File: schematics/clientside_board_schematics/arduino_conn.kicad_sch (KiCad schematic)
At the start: 1 part

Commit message: Assign footprints to RLCS Client-side board
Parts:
- XA1: footprint (none) -> rlcs_power_footprints:Arduino_Mega2560_Shield
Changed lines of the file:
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@@
       (effects (font (size 1.524 1.524)))
     )
-    (property "Footprint" "" (id 2) (at 163.83 18.415 0)
+    (property "Footprint" "rlcs_power_footprints:Arduino_Mega2560_Shield" (id 2) (at 163.83 18.415 0)
       (effects (font (size 1.524 1.524)) hide)
     )

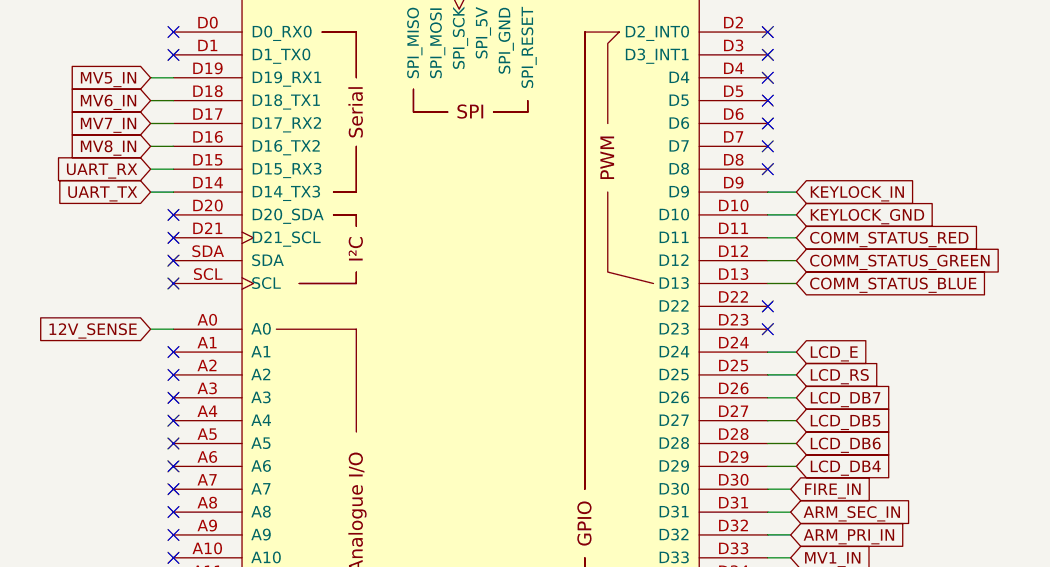
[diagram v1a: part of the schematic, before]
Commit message: Fix schematic issue on Client-side board
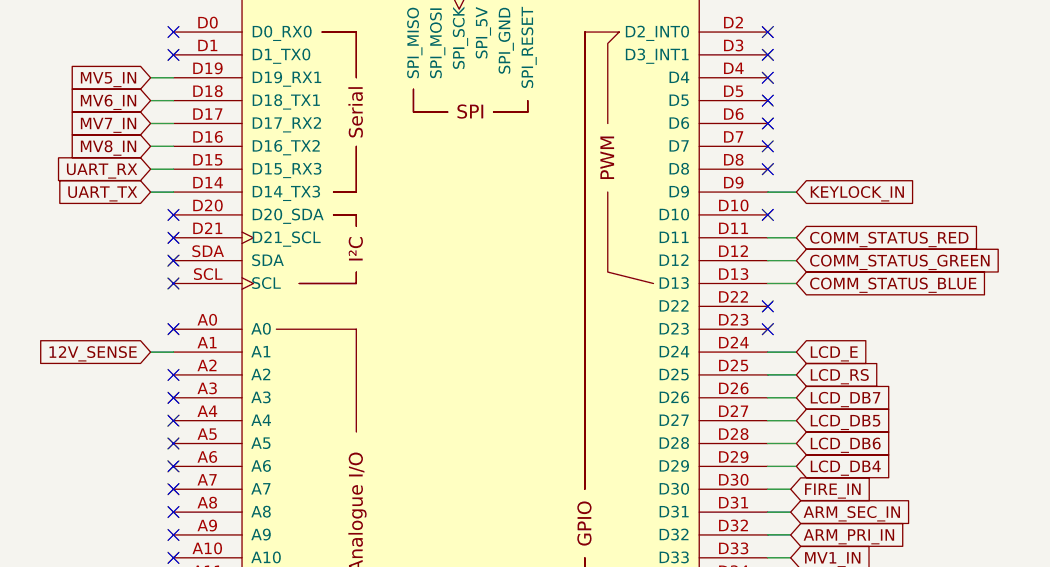
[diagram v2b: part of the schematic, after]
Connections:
- net 12V_SENSE: now also XA1.A1; no longer XA1.A0
- net KEYLOCK_GND: no longer names the net of XA1.D10
- no-connect marks 56 -> 57
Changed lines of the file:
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@@
   (no_connect (at 113.03 107.315))
   (no_connect (at 113.03 89.535))
-  (no_connect (at 113.03 69.215))
   (no_connect (at 113.03 53.975))
   (no_connect (at 179.07 36.195))
@@
   (no_connect (at 142.24 22.225))
   (no_connect (at 113.03 86.995))
+  (no_connect (at 113.03 66.675))
   (no_connect (at 179.07 117.475))
   (no_connect (at 179.07 140.335))
@@
   (no_connect (at 179.07 41.275))
   (no_connect (at 179.07 122.555))
+  (no_connect (at 179.07 53.975))
   (no_connect (at 113.03 104.775))
   (no_connect (at 179.07 43.815))
@@
     (stroke (width 0) (type default) (color 0 0 0 0))
   )
-  (wire (pts (xy 179.07 53.975) (xy 182.245 53.975))
-    (stroke (width 0) (type default) (color 0 0 0 0))
-  )
   (wire (pts (xy 108.585 135.255) (xy 108.585 137.795))
     (stroke (width 0) (type default) (color 0 0 0 0))
@@
     (stroke (width 0) (type default) (color 0 0 0 0))
   )
+  (wire (pts (xy 110.49 69.215) (xy 113.03 69.215))
+    (stroke (width 0) (type default) (color 0 0 0 0))
+  )
   (wire (pts (xy 179.07 59.055) (xy 182.245 59.055))
     (stroke (width 0) (type default) (color 0 0 0 0))
@@
     (stroke (width 0) (type default) (color 0 0 0 0))
   )
-  (wire (pts (xy 110.49 66.675) (xy 113.03 66.675))
-    (stroke (width 0) (type default) (color 0 0 0 0))
-  )
   (wire (pts (xy 108.585 137.795) (xy 108.585 140.335))
     (stroke (width 0) (type default) (color 0 0 0 0))
@@
     )
   )
-  (global_label "KEYLOCK_GND" (shape input) (at 182.245 53.975 0) (fields_autoplaced)
-    (effects (font (size 1.27 1.27)) (justify left))
-    (property "Intersheet References" "${INTERSHEET_REFS}" (id 0) (at 197.9024 53.8956 0)
-      (effects (font (size 1.27 1.27)) (justify left) hide)
-    )
-  )
   (global_label "ARM_SEC_IN" (shape input) (at 181.61 86.995 0) (fields_autoplaced)
     (effects (font (size 1.27 1.27)) (justify left))
@@
     )
   )
-  (global_label "12V_SENSE" (shape input) (at 110.49 66.675 180) (fields_autoplaced)
-    (effects (font (size 1.27 1.27)) (justify right))
-    (property "Intersheet References" "${INTERSHEET_REFS}" (id 0) (at 97.554 66.5956 0)
-      (effects (font (size 1.27 1.27)) (justify right) hide)
-    )
+  (global_label "12V_SENSE" (shape input) (at 110.49 69.215 180) (fields_autoplaced)
+    (effects (font (size 1.27 1.27)) (justify right))
+    (property "Intersheet References" "${INTERSHEET_REFS}" (id 0) (at 97.554 69.1356 0)
+      (effects (font (size 1.27 1.27)) (justify right) hide)
+    )

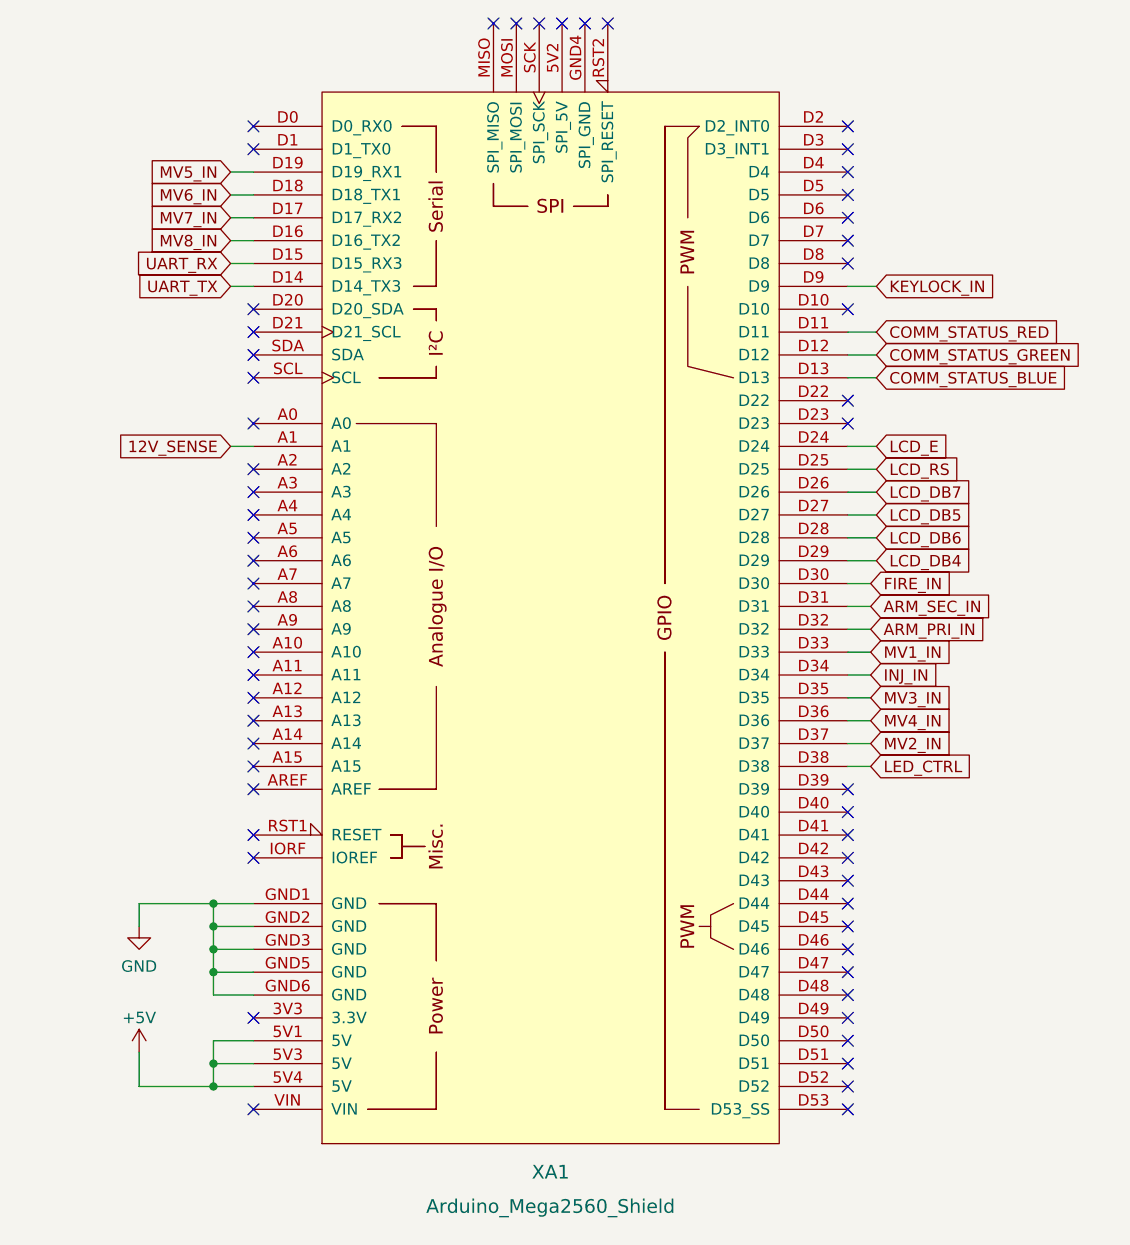
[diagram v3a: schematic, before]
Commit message: Update client-side board schematic
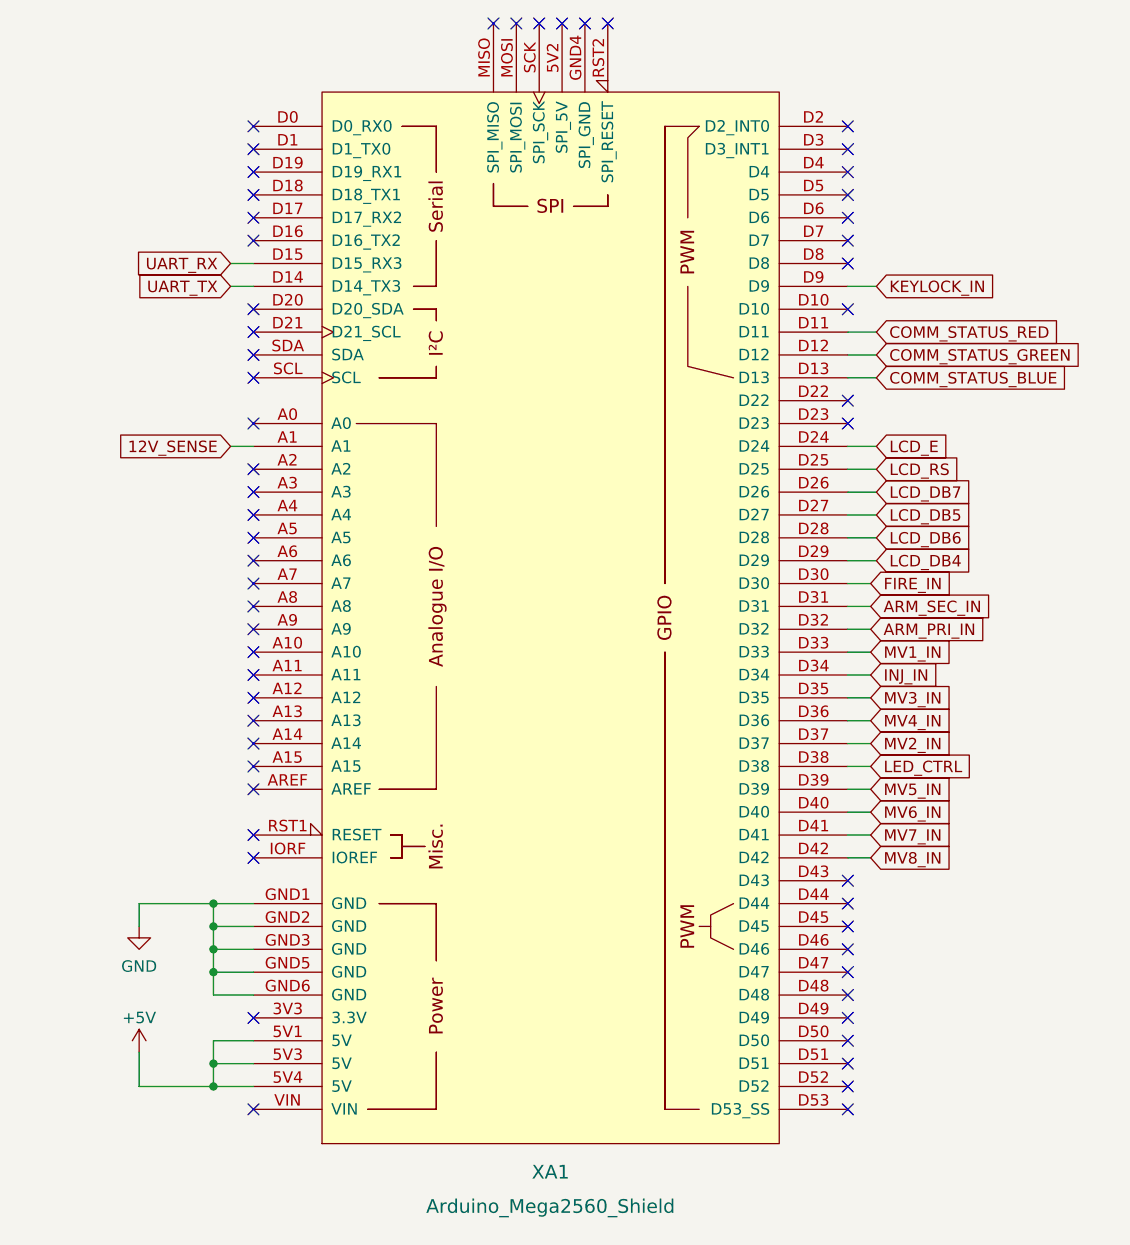
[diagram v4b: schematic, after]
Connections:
- net MV5_IN: now also XA1.D39; no longer XA1.D19 (D19_RX1)
- net MV6_IN: now also XA1.D40; no longer XA1.D18 (D18_TX1)
- net MV7_IN: now also XA1.D41; no longer XA1.D17 (D17_RX2)
- net MV8_IN: now also XA1.D42; no longer XA1.D16 (D16_TX2)
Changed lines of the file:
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@@
   (no_connect (at 113.03 59.055))
   (no_connect (at 179.07 127.635))
-  (no_connect (at 179.07 114.935))
   (no_connect (at 113.03 107.315))
   (no_connect (at 113.03 89.535))
@@
   (no_connect (at 179.07 48.895))
   (no_connect (at 147.32 22.225))
-  (no_connect (at 179.07 107.315))
   (no_connect (at 113.03 81.915))
   (no_connect (at 179.07 46.355))
   (no_connect (at 113.03 99.695))
-  (no_connect (at 179.07 112.395))
-  (no_connect (at 179.07 109.855))
   (no_connect (at 113.03 36.195))
   (no_connect (at 113.03 114.935))
@@
   (no_connect (at 179.07 142.875))
   (no_connect (at 179.07 41.275))
+  (no_connect (at 113.03 38.735))
   (no_connect (at 179.07 122.555))
+  (no_connect (at 113.03 43.815))
   (no_connect (at 179.07 53.975))
+  (no_connect (at 113.03 46.355))
   (no_connect (at 113.03 104.775))
   (no_connect (at 179.07 43.815))
   (no_connect (at 113.03 97.155))
   (no_connect (at 113.03 56.515))
+  (no_connect (at 113.03 41.275))
   (no_connect (at 113.03 71.755))
   (no_connect (at 179.07 33.655))
@@
   (no_connect (at 113.03 74.295))
   (no_connect (at 152.4 22.225))
-  (wire (pts (xy 110.49 38.735) (xy 113.03 38.735))
-    (stroke (width 0) (type default) (color 0 0 0 0))
-  )
   (wire (pts (xy 179.07 79.375) (xy 182.245 79.375))
     (stroke (width 0) (type default) (color 0 0 0 0))
@@
     (stroke (width 0) (type default) (color 0 0 0 0))
   )
+  (wire (pts (xy 179.07 112.395) (xy 181.61 112.395))
+    (stroke (width 0) (type default) (color 0 0 0 0))
+  )
   (wire (pts (xy 179.07 84.455) (xy 181.61 84.455))
     (stroke (width 0) (type default) (color 0 0 0 0))
@@
     (stroke (width 0) (type default) (color 0 0 0 0))
   )
-  (wire (pts (xy 110.49 43.815) (xy 113.03 43.815))
+  (wire (pts (xy 179.07 107.315) (xy 181.61 107.315))
     (stroke (width 0) (type default) (color 0 0 0 0))
   )
@@
     (stroke (width 0) (type default) (color 0 0 0 0))
   )
-  (wire (pts (xy 110.49 41.275) (xy 113.03 41.275))
-    (stroke (width 0) (type default) (color 0 0 0 0))
-  )
   (wire (pts (xy 108.585 127.635) (xy 113.03 127.635))
     (stroke (width 0) (type default) (color 0 0 0 0))
@@
     (stroke (width 0) (type default) (color 0 0 0 0))
   )
+  (wire (pts (xy 179.07 114.935) (xy 181.61 114.935))
+    (stroke (width 0) (type default) (color 0 0 0 0))
+  )
   (wire (pts (xy 179.07 97.155) (xy 181.61 97.155))
     (stroke (width 0) (type default) (color 0 0 0 0))
@@
     (stroke (width 0) (type default) (color 0 0 0 0))
   )
-  (wire (pts (xy 110.49 46.355) (xy 113.03 46.355))
-    (stroke (width 0) (type default) (color 0 0 0 0))
-  )
   (wire (pts (xy 108.585 140.335) (xy 100.33 140.335))
     (stroke (width 0) (type default) (color 0 0 0 0))
@@
     (stroke (width 0) (type default) (color 0 0 0 0))
   )
+  (wire (pts (xy 179.07 109.855) (xy 181.61 109.855))
+    (stroke (width 0) (type default) (color 0 0 0 0))
+  )
   (wire (pts (xy 108.585 137.795) (xy 108.585 140.335))
     (stroke (width 0) (type default) (color 0 0 0 0))
@@
     (stroke (width 0) (type default) (color 0 0 0 0))
   )
-  (global_label "MV5_IN" (shape input) (at 110.49 38.735 180) (fields_autoplaced)
-    (effects (font (size 1.27 1.27)) (justify right))
-    (property "Intersheet References" "${INTERSHEET_REFS}" (id 0) (at 101.4245 38.6556 0)
-      (effects (font (size 1.27 1.27)) (justify right) hide)
+  (global_label "MV5_IN" (shape input) (at 181.61 107.315 0) (fields_autoplaced)
+    (effects (font (size 1.27 1.27)) (justify left))
+    (property "Intersheet References" "${INTERSHEET_REFS}" (id 0) (at 190.6755 107.2356 0)
+      (effects (font (size 1.27 1.27)) (justify left) hide)
     )
   )
@@
     )
   )
-  (global_label "MV6_IN" (shape input) (at 110.49 41.275 180) (fields_autoplaced)
-    (effects (font (size 1.27 1.27)) (justify right))
-    (property "Intersheet References" "${INTERSHEET_REFS}" (id 0) (at 101.4245 41.1956 0)
-      (effects (font (size 1.27 1.27)) (justify right) hide)
+  (global_label "MV6_IN" (shape input) (at 181.61 109.855 0) (fields_autoplaced)
+    (effects (font (size 1.27 1.27)) (justify left))
+    (property "Intersheet References" "${INTERSHEET_REFS}" (id 0) (at 190.6755 109.7756 0)
+      (effects (font (size 1.27 1.27)) (justify left) hide)
     )
   )
@@
     )
   )
-  (global_label "MV7_IN" (shape input) (at 110.49 43.815 180) (fields_autoplaced)
-    (effects (font (size 1.27 1.27)) (justify right))
-    (property "Intersheet References" "${INTERSHEET_REFS}" (id 0) (at 101.4245 43.7356 0)
-      (effects (font (size 1.27 1.27)) (justify right) hide)
+  (global_label "MV7_IN" (shape input) (at 181.61 112.395 0) (fields_autoplaced)
+    (effects (font (size 1.27 1.27)) (justify left))
+    (property "Intersheet References" "${INTERSHEET_REFS}" (id 0) (at 190.6755 112.3156 0)
+      (effects (font (size 1.27 1.27)) (justify left) hide)
     )
   )
@@
     )
   )
-  (global_label "MV8_IN" (shape input) (at 110.49 46.355 180) (fields_autoplaced)
-    (effects (font (size 1.27 1.27)) (justify right))
-    (property "Intersheet References" "${INTERSHEET_REFS}" (id 0) (at 101.4245 46.2756 0)
-      (effects (font (size 1.27 1.27)) (justify right) hide)
+  (global_label "MV8_IN" (shape input) (at 181.61 114.935 0) (fields_autoplaced)
+    (effects (font (size 1.27 1.27)) (justify left))
+    (property "Intersheet References" "${INTERSHEET_REFS}" (id 0) (at 190.6755 114.8556 0)
+      (effects (font (size 1.27 1.27)) (justify left) hide)
     )
   )
@@
   (symbol (lib_id "power:+5V") (at 100.33 136.525 0) (unit 1)
     (in_bom yes) (on_board yes)
-    (property "Reference" "#PWR0102" (id 0) (at 100.33 140.335 0)
+    (property "Reference" "#PWR030" (id 0) (at 100.33 140.335 0)
       (effects (font (size 1.27 1.27)) hide)
     )
@@
   (symbol (lib_id "power:GND") (at 100.33 122.555 0) (unit 1)
     (in_bom yes) (on_board yes)
-    (property "Reference" "#PWR0101" (id 0) (at 100.33 128.905 0)
+    (property "Reference" "#PWR029" (id 0) (at 100.33 128.905 0)
       (effects (font (size 1.27 1.27)) hide)
     )

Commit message: Update Client-side board schematic for reduce routing complexity
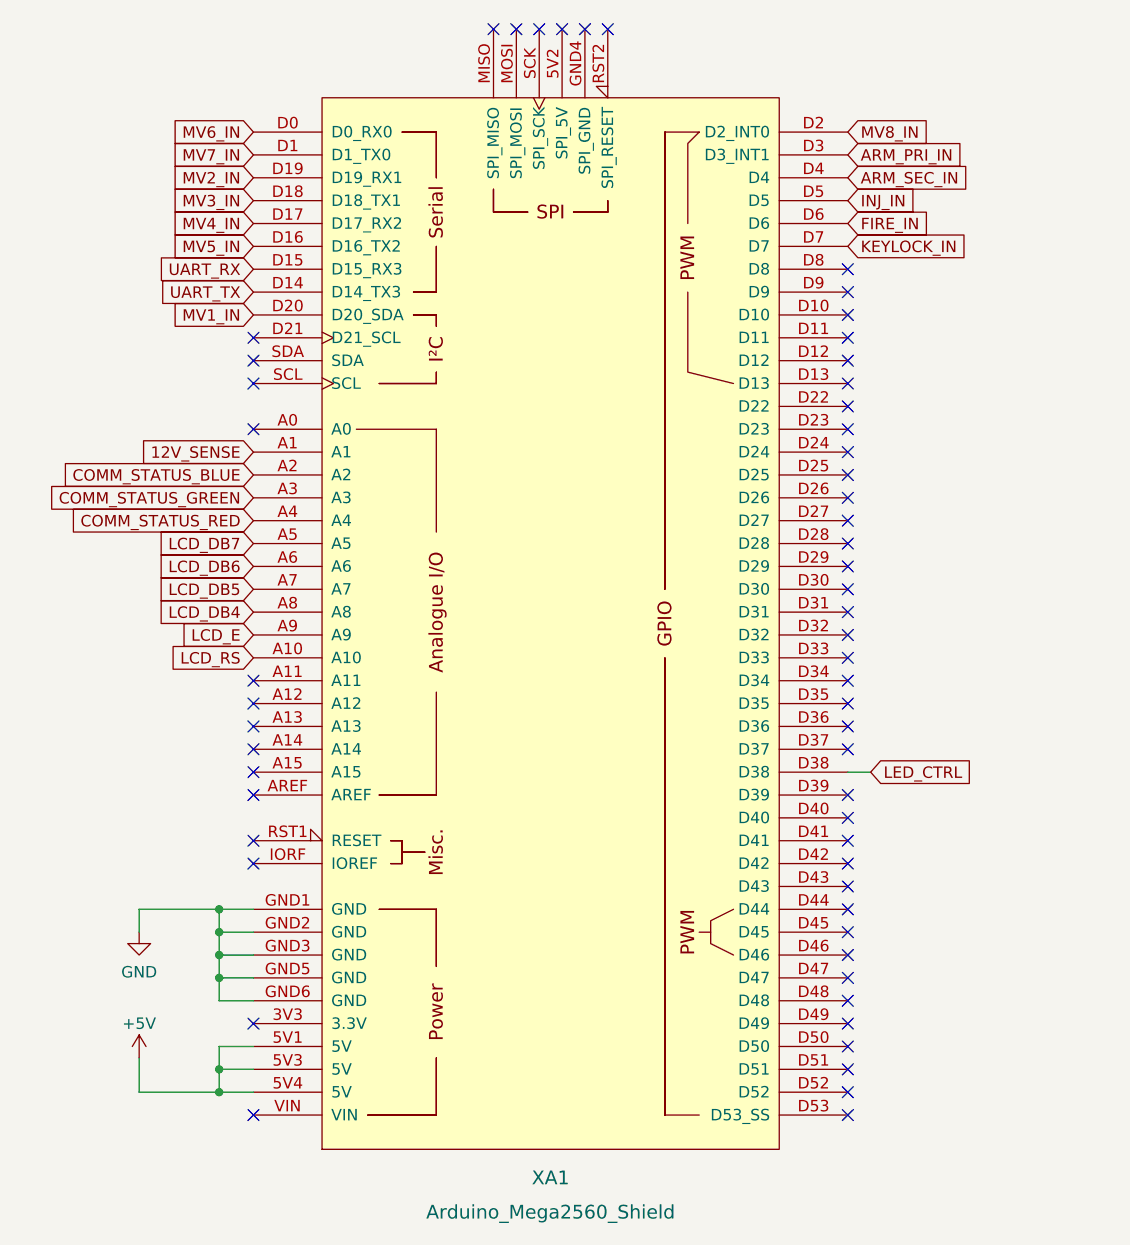
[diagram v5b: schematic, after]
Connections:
- net ARM_PRI_IN: now also XA1.D3 (D3_INT1); no longer XA1.D32
- net ARM_SEC_IN: now also XA1.D4; no longer XA1.D31
- net COMM_STATUS_BLUE: now also XA1.A2; no longer XA1.D13
- net COMM_STATUS_GREEN: now also XA1.A3; no longer XA1.D12
- net COMM_STATUS_RED: now also XA1.A4; no longer XA1.D11
- net FIRE_IN: now also XA1.D6; no longer XA1.D30
- net INJ_IN: now also XA1.D5; no longer XA1.D34
- net KEYLOCK_IN: now also XA1.D7; no longer XA1.D9
- net LCD_DB4: now also XA1.A8; no longer XA1.D29
- net LCD_DB5: now also XA1.A7; no longer XA1.D27
- net LCD_DB6: now also XA1.A6; no longer XA1.D28
- net LCD_DB7: now also XA1.A5; no longer XA1.D26
- net LCD_E: now also XA1.A9; no longer XA1.D24
- net LCD_RS: now also XA1.A10; no longer XA1.D25
- net MV1_IN: now also XA1.D20 (D20_SDA); no longer XA1.D33
- net MV2_IN: now also XA1.D19 (D19_RX1); no longer XA1.D37
- net MV3_IN: now also XA1.D18 (D18_TX1); no longer XA1.D35
- net MV4_IN: now also XA1.D17 (D17_RX2); no longer XA1.D36
- net MV5_IN: now also XA1.D16 (D16_TX2); no longer XA1.D39
- net MV6_IN: now also XA1.D0 (D0_RX0); no longer XA1.D40
- net MV7_IN: now also XA1.D1 (D1_TX0); no longer XA1.D41
- net MV8_IN: now also XA1.D2 (D2_INT0); no longer XA1.D42
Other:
- moved on the sheet: XA1
